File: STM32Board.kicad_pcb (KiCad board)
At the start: 2 copper layers, 40 x 40 mm, 28 parts, among them J1 Conn_01x03_Male, J2 Conn_01x03_Male, J3 Conn_01x06_Male, J4 Conn_01x04_Male, J7 Conn_01x02_Male, J8 USB4105-GF-A, J9 USB4105-GF-A, SW1 SW_Push, SW2 SW_DIP_x01, U1 STM32F103C8Tx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

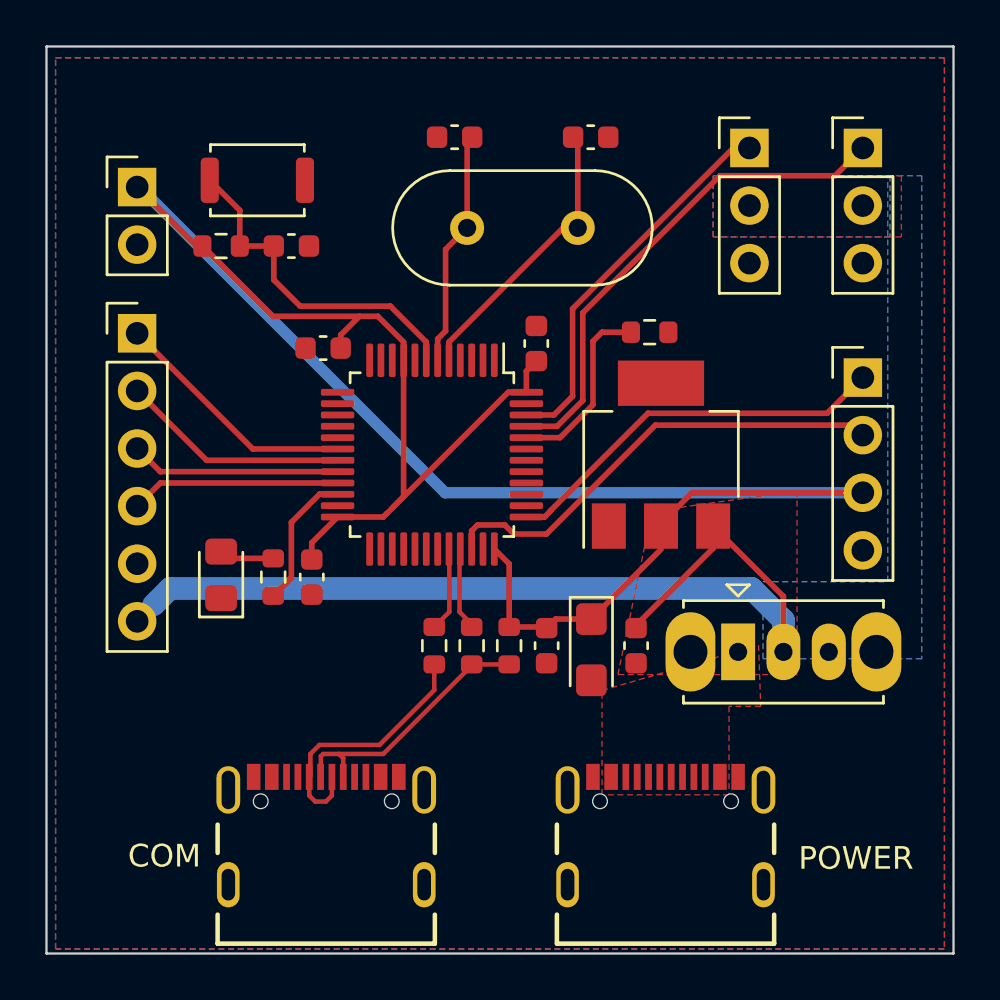
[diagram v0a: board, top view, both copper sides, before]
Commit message: add gitignore file and repair error in schematics
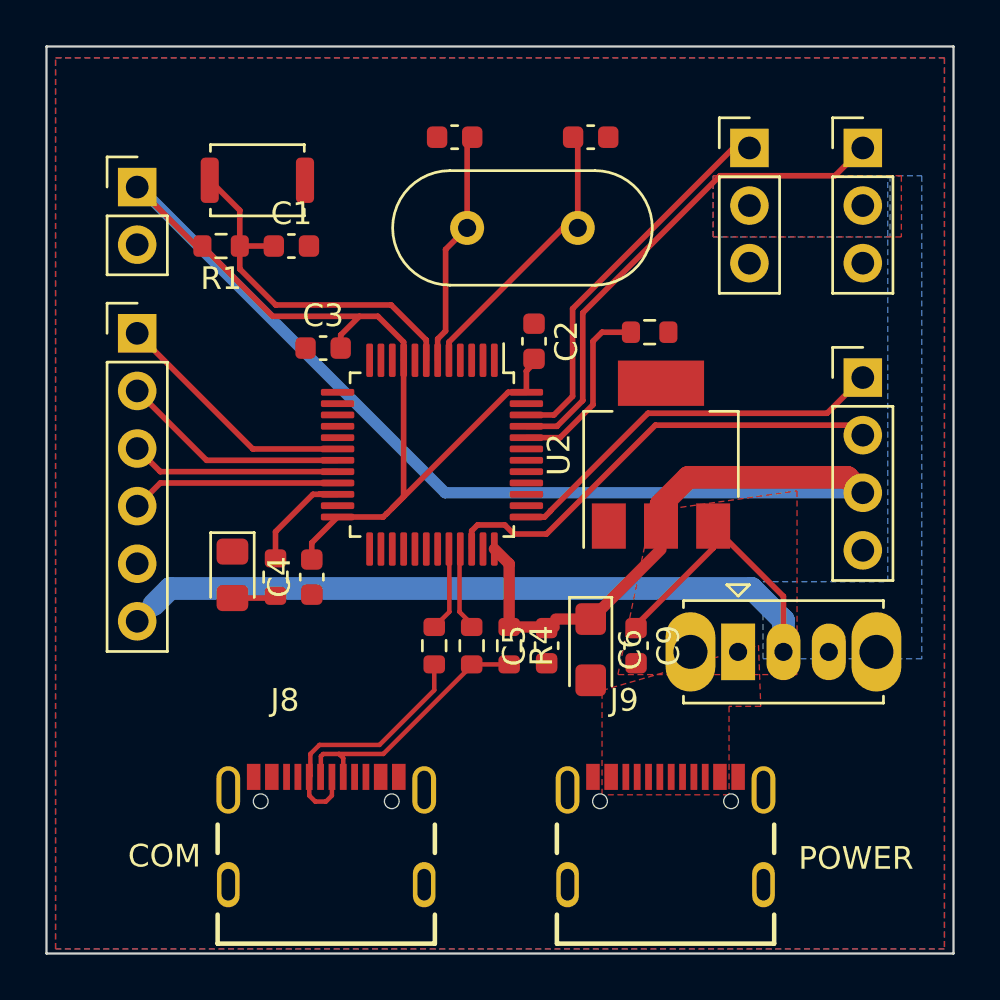
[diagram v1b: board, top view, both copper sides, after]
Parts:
- C5: value 10u -> 0.1uF
- C6: value 22u -> 22uF
- C9: value 0.1uF -> 10uF
- U2: footprint Package_TO_SOT_SMD:SOT-223 -> Package_TO_SOT_SMD:SOT-223-3_TabPin2
- moved C9 19.0 mm to (119.0, 119.4), turned to -90 degrees
- moved C2 13.4 mm to (114.5, 106.0)
- moved C3 9.40 mm to (105.2, 106.3), turned to 0 degrees
- moved C5 3.94 mm to (115.1, 119.4), turned to 90 degrees
- moved D1 0.50 mm to (101.2, 116.3), turned to -90 degrees
- moved R3 0.10 mm to (103.1, 116.4), turned to -90 degrees
- turned C1 to 0 degrees
- turned C4 to 90 degrees
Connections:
- C1 pad 1: GND -> Net-(R1-Pad1)
- C1 pad 2: Net-(C1-Pad2) -> GND
- C2 pad 1: +3V3 -> GND
- C2 pad 2: GND -> +3V3
- C3 pad 1: +3V3 -> GND
- C3 pad 2: GND -> +3V3
- C4 pad 1: +3V3 -> GND
- C4 pad 2: GND -> +3V3
- C5 pad 1: +5V -> GND
- C5 pad 2: GND -> +3V3
- C9 pad 1: +3V3 -> +5V
- J8 pad B4_A9: unconnected-(J8-PadA4_B9) -> unconnected-(J8-PadB4_A9)
- R1 pad 1: Net-(C1-Pad2) -> Net-(R1-Pad1)
- SW1 pad 1: Net-(C1-Pad2) -> Net-(R1-Pad1)
- U1 pad 7: Net-(C1-Pad2) -> Net-(R1-Pad1)
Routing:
- net Net-(R1-Pad1): track 0.00 -> 16.4 mm
- net Net-(C1-Pad2): track 15.1 -> 0.00 mm
- net +3V3: track 97.4 -> 98.5 mm
- net Net-(R3-Pad1): track 6.14 -> 5.40 mm

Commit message: Add gerber file, change the 3.3 and gnd def
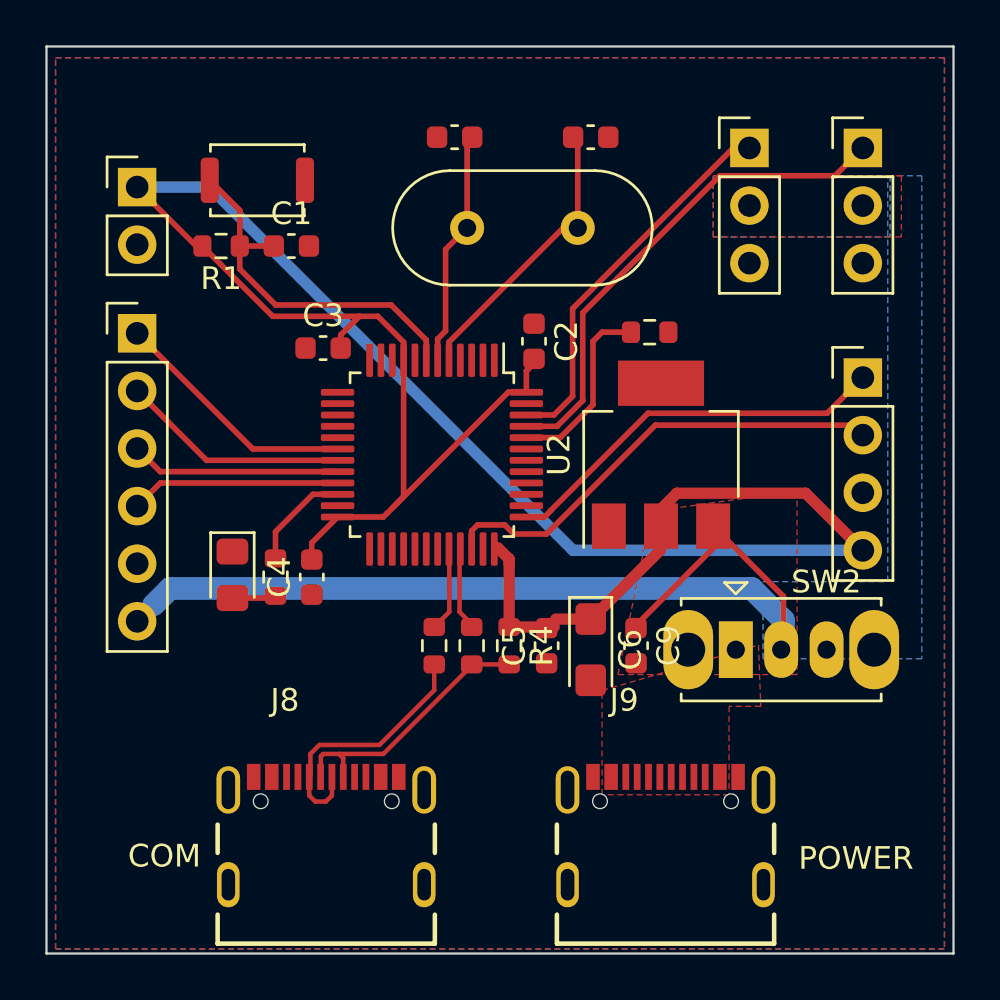
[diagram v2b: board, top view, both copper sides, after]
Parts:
- C7, C8: value 27pF -> 30pF
- SW2: value SW_DIP_x01 -> SW_SPDT
- U2: footprint Package_TO_SOT_SMD:SOT-223-3_TabPin2 -> Package_TO_SOT_SMD:SOT-223
- moved SW2 0.14 mm to (123.4, 119.6)
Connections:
- J4 pad 3: +3V3 -> GND
- J4 pad 4: GND -> +3V3
- SW2 pad 3: (no net) -> unconnected-(SW2-Pad3)
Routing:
- net +3V3: track 98.5 -> 99.9 mm
- net Net-(R3-Pad1): track 5.40 -> 4.60 mm
